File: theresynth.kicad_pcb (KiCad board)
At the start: 2 copper layers, 214 x 69.7 mm, 153 parts, among them J1 AudioJack3_Switch, J2 AudioJack2, J3 AudioJack2, J4 AudioJack2, J5 Jack-12V AC, J6 Ext. GND, J7 To_Amp, Q1 2N3904, Q2 2N3904, Q3 2N3904, Q4 2N3904, Q5 2N3904, Q6 J113, Q7 2N3904, SW1 SW_SPST, U1 TL074, U2 TL074, U3 TL072, U4 LM7812_TO220, U5 LM7912_TO220

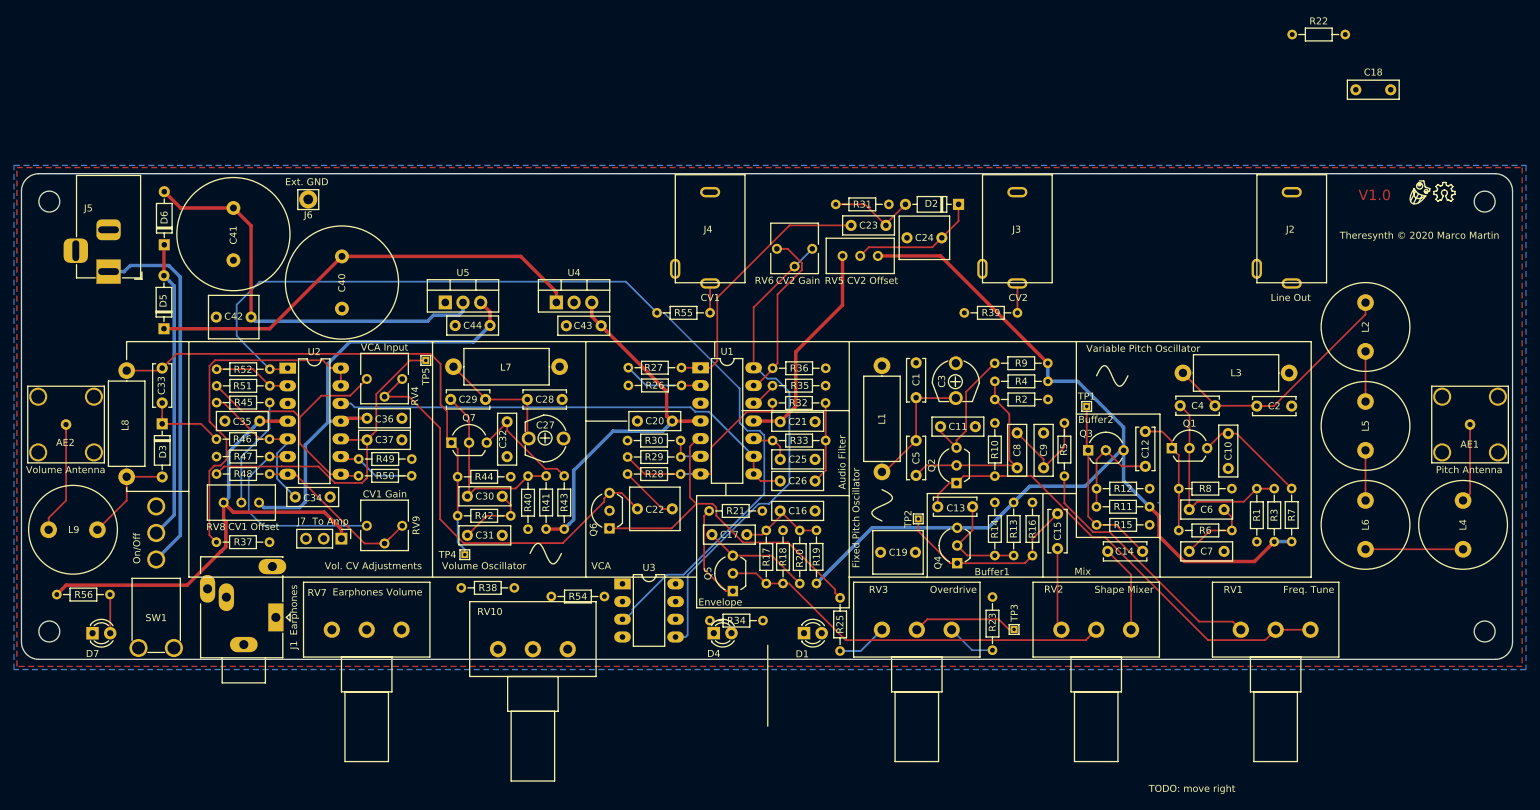
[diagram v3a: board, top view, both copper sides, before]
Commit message: full connection before relayouting labels
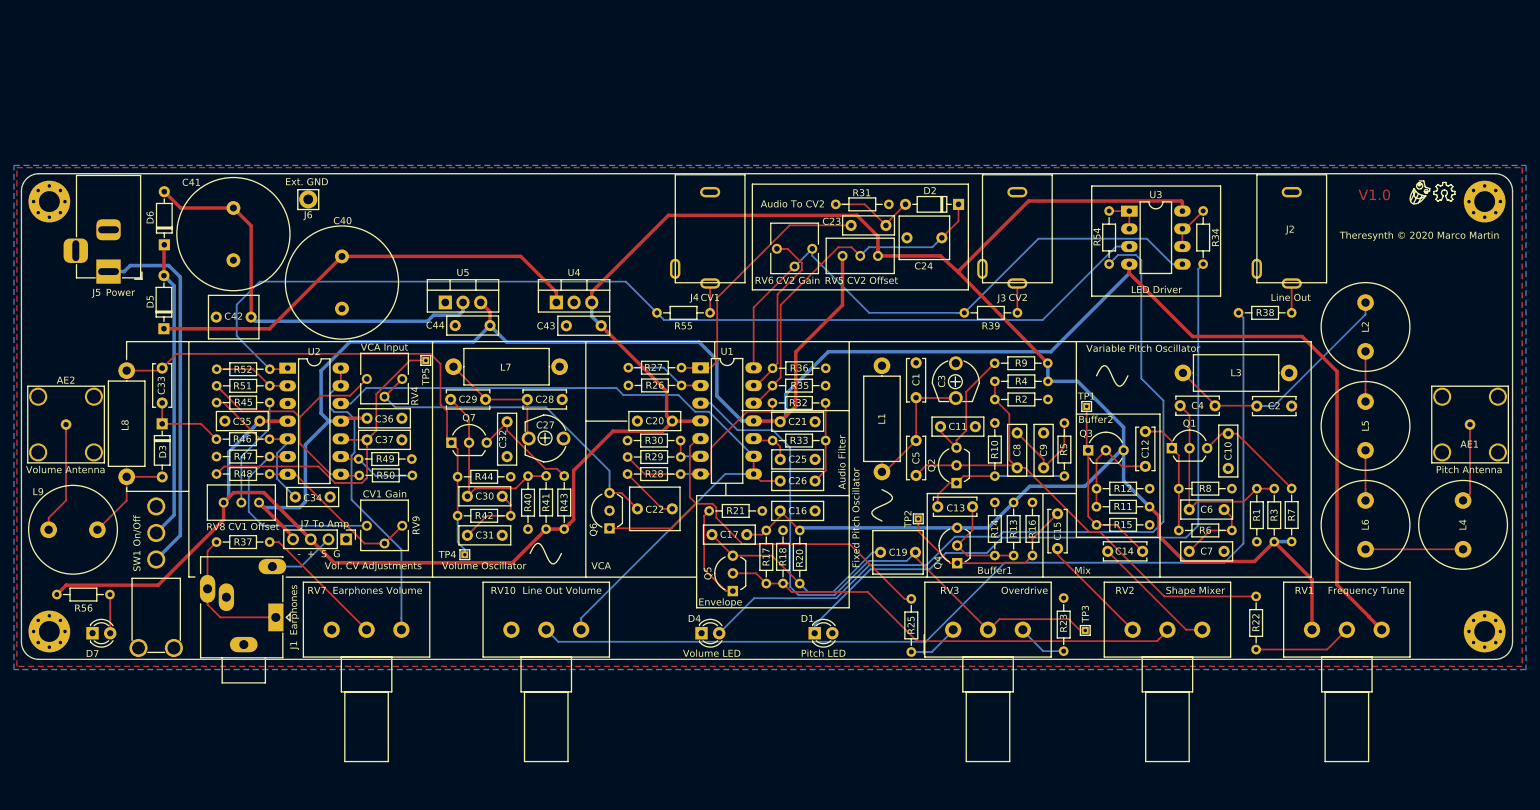
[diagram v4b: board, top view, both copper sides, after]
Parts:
- removed C18: 10n, Capacitor_THT:C_Rect_L7.2mm_W2.5mm_P5.00mm_FKS2_FKP2_MKS2_MKP2
- removed R19: 1k, Resistor_THT:R_Axial_DIN0204_L3.6mm_D1.6mm_P7.62mm_Horizontal
- ? (x4): footprint MountingHole:MountingHole_3mm -> MountingHole:MountingHole_3mm_Pad_Via
- J7: footprint Connector_PinHeader_2.54mm:PinHeader_1x03_P2.54mm_Vertical -> Connector_PinHeader_2.54mm:PinHeader_1x04_P2.54mm_Vertical
- R17: value 260k -> 470k
- R18: value 100k -> 47k
- R20: value 6.8k -> 10k
- R22: value 2.2k -> 1M
- R23: value 10k -> 22k
- R5: value 220 -> 1k
- RV1: value 1k -> 100k
- moved R38 118.3 mm to (226.3, 79.8)
- moved R54 93.2 mm to (200.1, 72.8), turned to 90 degrees
- moved U3 90.3 mm to (203.0, 65.2)
- moved R34 81.3 mm to (213.6, 72.8), turned to 90 degrees
- moved R22 80.8 mm to (221.2, 120.5), turned to 270 degrees
- moved R23 10.2 mm to (193.6, 128.3)
- moved R25 10.2 mm to (171.7, 120.8)
- moved TP3 10.2 mm to (196.7, 125.3)
- moved RV1 10.2 mm to (229.2, 125.2)
- moved RV2 10.2 mm to (203.5, 125.2)
- moved RV3 10.2 mm to (177.7, 125.2)
- moved R37 7.60 mm to (72.0, 112.7), turned to 0 degrees
- moved RV10 3.39 mm to (114.3, 125.2)
- moved D4 1.76 mm to (141.6, 125.8)
- moved D1 1.53 mm to (157.8, 125.8)
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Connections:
- net VolumeControlOut renamed /Volume Control/VolumeControlOut
- C16 pad 1: Net-(C16-Pad1) -> +12V
- C17 pad 1: Net-(C16-Pad1) -> +12V
- C19 pad 2: Net-(C18-Pad1) -> Net-(C17-Pad2)
- J7 pad 1: +12V -> GND
- J7 pad 2: GND -> Net-(J1-PadTN)
- J7 pad 3: Net-(J1-PadTN) -> +12V
- R17 pad 1: Net-(C16-Pad1) -> +12V
- R20 pad 1: Net-(C16-Pad1) -> +12V
- R22 pad 1: Net-(C17-Pad2) -> Net-(C5-Pad1)
- R22 pad 2: Net-(C18-Pad1) -> Net-(R22-Pad2)
- R37 pad 1: Net-(R37-Pad1) -> Net-(J1-PadR)
- R38 pad 1: Net-(R38-Pad1) -> Net-(J2-PadT)
- R38 pad 2: Net-(C26-Pad1) -> Net-(R38-Pad2)
- R5 pad 1: Net-(R5-Pad1) -> Net-(C13-Pad2)
- RV1 pad 1: Net-(R5-Pad1) -> +12V
- RV1 pad 2: Net-(C13-Pad2) -> Net-(R22-Pad2)
- RV1 pad 3: Net-(C13-Pad2) -> -12V
- RV10 pad 2: Net-(R38-Pad1) -> Net-(R38-Pad2)
- RV10 pad 3: Net-(J2-PadT) -> Net-(C26-Pad1)
- RV7 pad 2: Net-(R37-Pad1) -> Net-(R37-Pad2)
- RV7 pad 3: Net-(J1-PadR) -> Net-(RV7-Pad3)
- U2 pad 13: Net-(R37-Pad2) -> Net-(RV7-Pad3)
- U2 pad 14: Net-(R37-Pad2) -> Net-(RV7-Pad3)
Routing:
- net -12V: track 95.5 -> 288.9 mm
- net +12V: track 264.6 -> 408.3 mm
- net Net-(R38-Pad2): track 0.00 -> 140.0 mm
- net Net-(D4-Pad2): track 0.00 -> 114.7 mm
- net Net-(D1-Pad1): track 0.00 -> 99.9 mm
- net Net-(C19-Pad1): track 15.2 -> 87.2 mm
- net Net-(C13-Pad2): track 66.7 -> 21.0 mm
- net Net-(RV7-Pad3): track 0.00 -> 44.4 mm
- net Net-(C5-Pad1): track 29.0 -> 70.9 mm
- net Net-(C26-Pad1): track 69.8 -> 106.7 mm
- net Net-(R5-Pad1): track 36.7 -> 0.00 mm
- net Net-(R37-Pad2): track 50.7 -> 19.1 mm
- net Net-(C24-Pad1): track 22.5 -> 49.9 mm
- net Net-(J1-PadR): track 0.00 -> 20.1 mm
- net Net-(C17-Pad2): track 15.5 -> 30.0 mm
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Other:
- board text added: "- + S G"
- board text added: "Audio To CV2"
- board text added: "Frequency Tune"
- board text added: "JLCJLCJLCJLC"
- board text added: "LED Driver"
- board text added: "Line Out Volume"
- board text added: "Pitch LED"
- board text added: "Power"
- board text added: "Volume LED"
- board text removed: "Freq. Tune"
- board text removed: "TODO: move right"

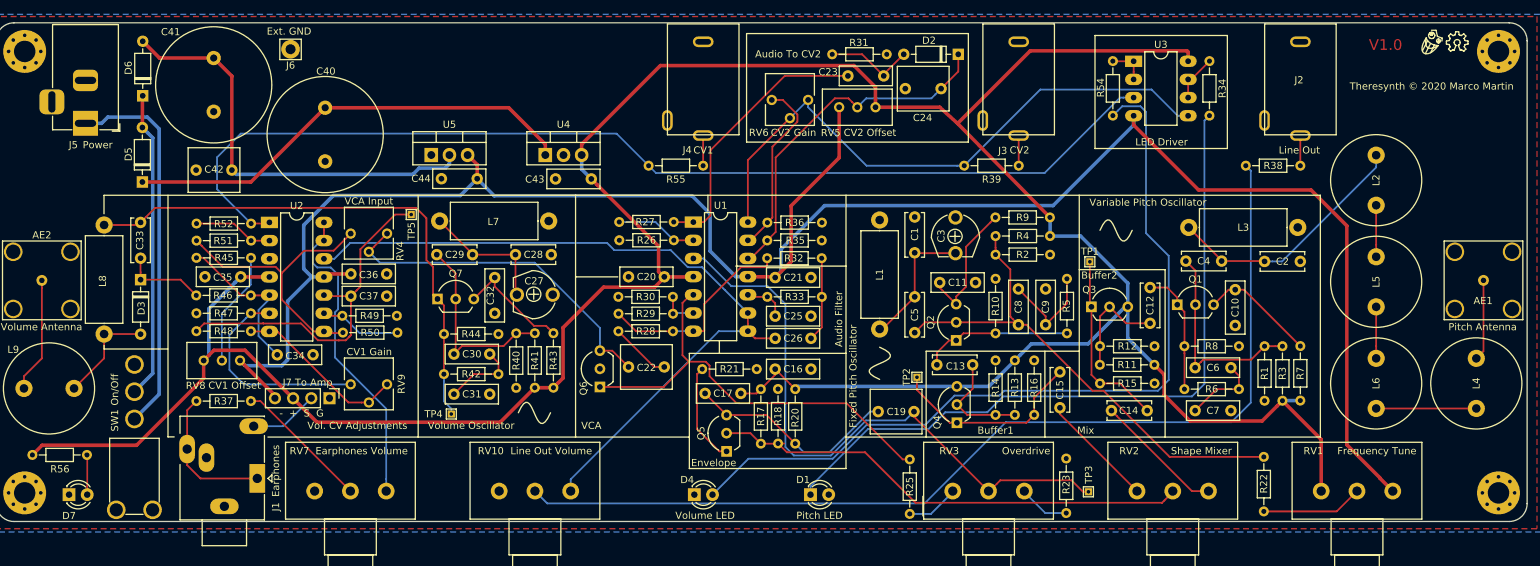
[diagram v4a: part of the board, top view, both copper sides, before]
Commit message: migrate audio processing to new sheet
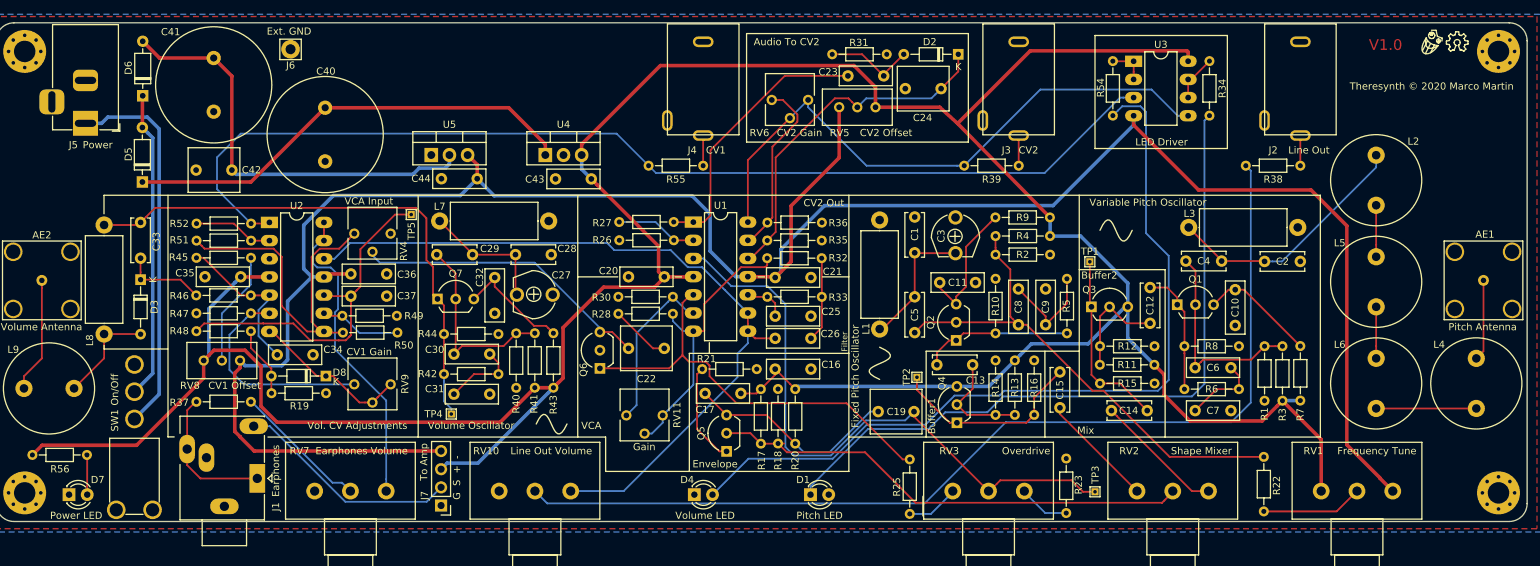
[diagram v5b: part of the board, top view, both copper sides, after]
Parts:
- removed R29: 100k, Resistor_THT:R_Axial_DIN0204_L3.6mm_D1.6mm_P7.62mm_Horizontal
- added D8: 1N4148, Diode_THT:D_DO-34_SOD68_P7.62mm_Horizontal, F.Cu at (90.1, 109.2)
- added R19: 100k, Resistor_THT:R_Axial_DIN0204_L3.6mm_D1.6mm_P7.62mm_Horizontal, F.Cu at (82.5, 111.6)
- added RV11: 100k, Potentiometer_THT:Potentiometer_Vishay_T73YP_Vertical, F.Cu at (132.1, 114.7)
- C23: value 10n -> 2.2n
- D2, D3: footprint Diode_THT:D_DO-35_SOD27_P7.62mm_Horizontal -> Diode_THT:D_DO-34_SOD68_P7.62mm_Horizontal
- R22: value 1M -> 330k
- R25: value 22k -> 220k
- R31: value 100k -> 10k
- moved J7 21.6 mm to (106.2, 127.3), turned to 180 degrees
- moved C22 2.60 mm to (137.4, 105.3)
- moved Q6 2.60 mm to (128.4, 108.1)
- moved R28 2.44 mm to (138.6, 100.5)
- moved TP3 0.92 mm to (197.6, 125.3)
- moved RV4 0.50 mm to (94.1, 89.3)
- moved RV9 0.50 mm to (94.1, 110.3)
- moved R37 0.10 mm to (72.0, 112.8)
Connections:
- net /Volume Control/VolumeControlOut renamed /Audio Processing/VolumeControlIn
- net Net-(C17-Pad2) renamed /Audio Processing/RawAudioIn
- R48 pad 2: Net-(R48-Pad2) -> Net-(D8-Pad2)
- RV4 pad 3: Net-(C22-Pad2) -> GND
- RV9 pad 2: Net-(R48-Pad2) -> Net-(D8-Pad1)
- RV9 pad 3: Net-(R48-Pad2) -> Net-(D8-Pad1)
- U2 pad 7: Net-(R48-Pad2) -> Net-(D8-Pad1)
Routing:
- net -12V: track 288.9 -> 321.8 mm
- net Net-(R48-Pad2): track 24.2 -> 0.00 mm
- net +12V: track 408.3 -> 432.0 mm
- net Net-(D8-Pad1): track 0.00 -> 22.6 mm
- net Net-(J1-PadTN): track 10.5 -> 32.2 mm
- net Net-(R30-Pad1): track 5.14 -> 23.1 mm
- net Net-(R28-Pad1): track 28.8 -> 39.5 mm
- net Net-(D8-Pad2): track 0.00 -> 9.92 mm
- net /Audio Processing/VolumeControlIn: track 39.8 -> 48.8 mm
- net Net-(C22-Pad2): track 48.4 -> 41.6 mm
- net Net-(C26-Pad1): track 106.7 -> 108.6 mm
- net Net-(Q6-Pad1): track 61.9 -> 60.3 mm
- net Net-(C19-Pad1): track 87.2 -> 88.1 mm
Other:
- board text added: "CV2 Out"
- board text added: "Filter"
- board text added: "G S + -"
- board text added: "Gain"
- board text added: "Power LED"
- board text removed: "- + S G"
- board text removed: "Audio Filter"

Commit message: 1.0 for fabrication
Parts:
- R36: value 1k -> 10k
- R43: renamed from R45; value 220k -> 330k
- RV11, RV4, RV9: footprint Potentiometer_THT:Potentiometer_Vishay_T73YP_Vertical -> Potentiometer_THT:Potentiometer_Bourns_3386P_Vertical
- RV6: value 10k -> 100k; footprint Potentiometer_THT:Potentiometer_Vishay_T73YP_Vertical -> Potentiometer_THT:Potentiometer_Bourns_3386P_Vertical
- moved TP5 10.7 mm to (91.4, 85.0), turned to 0 degrees
- moved RV4 1.63 mm to (95.2, 88.1)
- moved RV6 1.55 mm to (151.6, 69.3)
- moved C40 1.35 mm to (90.5, 70.4)
- moved RV9 0.91 mm to (95.0, 110.3)
- moved RV11 0.86 mm to (132.5, 115.4)
- renumbered C27 to C18, C28 to C27, C29 to C28, C30 to C29, C31 to C30, C32 to C31, C33 to C32, C34 to C33, C37 to C34, D8 to D4, D4 to D8, R40 to R19, R41 to R24, R42 to R29, R43 to R40, R44 to R41, R46 to R42, R47 to R44, R19 to R45, R48 to R46, R49 to R47, R50 to R48, R51 to R49, R52 to R50, R55 to R51, R54 to R52
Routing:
- net Net-(R36-Pad2): track 25.1 -> 28.6 mm
- net Net-(D1-Pad1): track 99.9 -> 97.1 mm
- net Net-(R39-Pad2): track 84.4 -> 87.0 mm
- net Net-(R50-Pad2): track 150.0 -> 152.3 mm
- net Net-(C23-Pad2): track 38.2 -> 40.5 mm
- net /Audio Processing/VolumeControlIn: track 48.8 -> 50.5 mm
- net Net-(C32-Pad1): track 75.5 -> 76.9 mm
- net Net-(R44-Pad2): track 29.5 -> 30.9 mm
- net Net-(C22-Pad2): track 41.6 -> 40.4 mm
- net Net-(C34-Pad1): track 49.0 -> 50.2 mm
- net Net-(C41-Pad2): track 60.1 -> 61.2 mm
- net Net-(D4-Pad1): track 22.6 -> 23.5 mm
- net Net-(C31-Pad2): track 16.4 -> 17.3 mm
- net Net-(C26-Pad1): track 108.6 -> 109.5 mm
- net Net-(C40-Pad1): track 64.2 -> 65.1 mm
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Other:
- board text added: "Vol. CV"
- board text removed: "Vol. CV Adjustments"

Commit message: add panels
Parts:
- removed C42: 1u, Capacitor_THT:C_Rect_L7.0mm_W6.0mm_P5.00mm
- C14, C15: value 10p -> 22p
- C31: value 100p -> 100n
- C4: value 100p -> 220p
- C40, C41: value 4700u -> 3300u; footprint Capacitor_THT:C_Radial_D16.0mm_H31.5mm_P7.50mm -> Capacitor_THT:CP_Radial_D13.0mm_P5.00mm
- C5: value 100p -> 330p
- L1, L3: value 4.8mH -> 4.7mH
- L8: value 4.8m -> 1m
- R26, R36: value 10k -> 1k
- RV10, RV7: value 100k -> 10k
- moved TP3 29.7 mm to (168.1, 128.4)
- moved C41 2.15 mm to (74.4, 70.1)
- moved C40 0.65 mm to (90.6, 71.1)
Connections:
- RV3 pad 1: Net-(R25-Pad2) -> Net-(R23-Pad1)
- RV3 pad 2: Net-(C19-Pad1) -> Net-(R25-Pad2)
- RV3 pad 3: Net-(R23-Pad1) -> Net-(C19-Pad1)
- RV7 pad 2: Net-(R37-Pad2) -> Net-(RV7-Pad2)
- RV7 pad 3: Net-(RV7-Pad3) -> Net-(C26-Pad1)
- TP3 pad 1: Net-(C19-Pad1) -> Net-(R25-Pad2)
- U2 pad 12: Net-(C26-Pad1) -> Net-(RV7-Pad2)
- U2 pad 13: Net-(RV7-Pad3) -> Net-(R37-Pad2)
- U2 pad 14: Net-(RV7-Pad3) -> Net-(R37-Pad2)
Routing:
- net Net-(RV7-Pad2): track 0.00 -> 54.0 mm
- net GND: track 0.11 -> 48.0 mm
- net Net-(RV7-Pad3): track 44.5 -> 0.00 mm
- net Net-(C26-Pad1): track 109.5 -> 72.3 mm
- net Net-(R37-Pad2): track 19.1 -> 44.6 mm
- net Net-(R50-Pad2): track 152.3 -> 137.9 mm
- net Net-(C41-Pad2): track 61.2 -> 49.7 mm
- net Net-(R23-Pad1): track 7.07 -> 18.4 mm
- net Net-(C19-Pad1): track 88.1 -> 78.6 mm
- net Net-(R25-Pad2): track 7.27 -> 16.0 mm
- net Net-(R38-Pad2): track 140.0 -> 137.9 mm
- net Net-(C5-Pad1): track 70.9 -> 72.2 mm
- net Net-(Q5-Pad2): track 67.9 -> 67.0 mm
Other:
- board text added: "V1.1"
- board text removed: "V1.0"
